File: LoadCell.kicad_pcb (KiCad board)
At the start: 2 copper layers, 50.8 x 18.5 mm, 44 parts, among them J1 M20-8760242, J2 0.100_1X4, J3 M20-8760242, J4 0.100_1X4, J5 M20-8760242, J6 0.100_1X4, J7 M20-8760242, J8 0.100_1X4, U1 L78L12ABUTR, U2 LM321SN3T1G, U3 L78L12ABUTR, U4 LM321SN3T1G, U5 L78L12ABUTR, U6 LM321SN3T1G, U7 L78L12ABUTR, U8 LM321SN3T1G

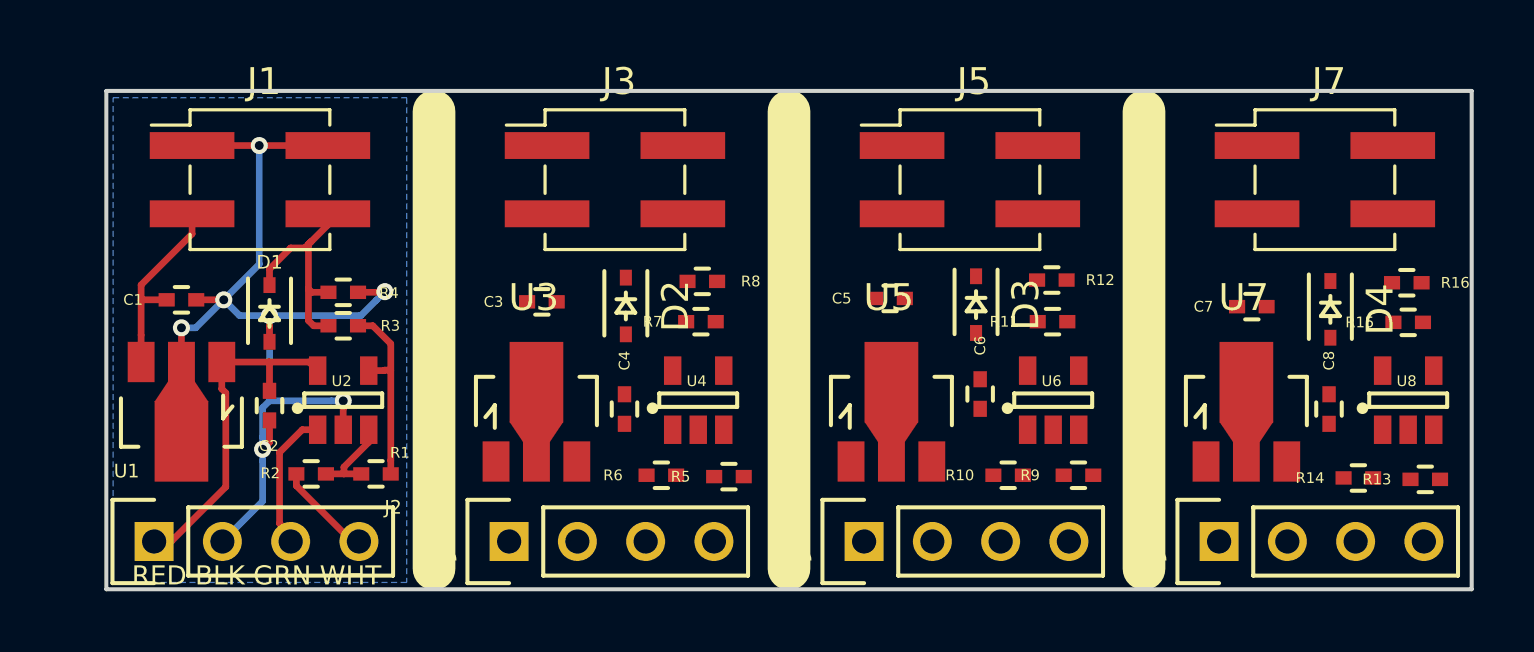
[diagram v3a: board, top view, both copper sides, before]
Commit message: Changed load cell termination pads
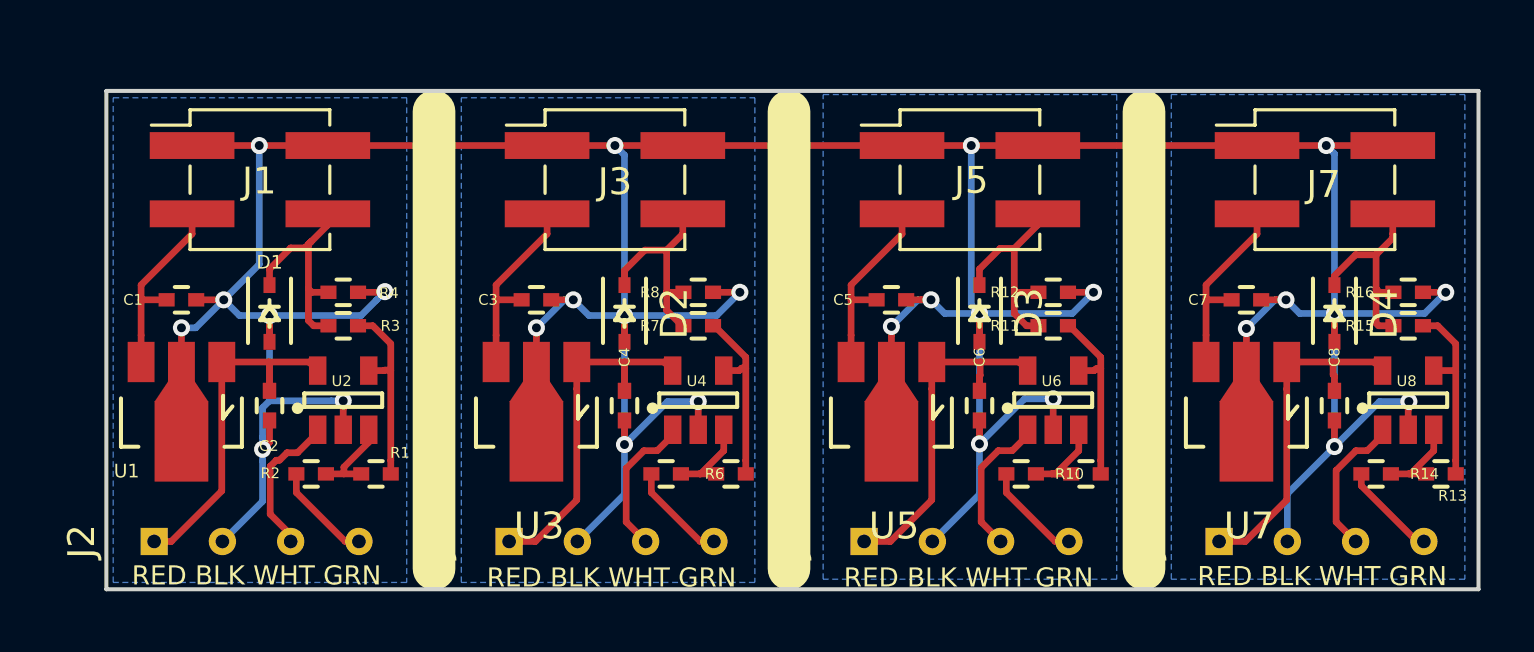
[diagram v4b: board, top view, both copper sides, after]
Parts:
- J2, J4, J6, J8: footprint _Connector:0.100_1x4_small -> _Connector:0.100_1x4_micro
- moved R14 0.68 mm to (148.8, 97.3), turned to 180 degrees
- moved R13 0.62 mm to (151.3, 97.3), turned to 180 degrees
- moved R10 0.49 mm to (135.6, 97.3), turned to 180 degrees
- moved R12 0.46 mm to (136.8, 90.6), turned to 0 degrees
- moved R8 0.43 mm to (123.6, 90.6), turned to 0 degrees
- moved C6 0.43 mm to (134.1, 94.8)
- moved R16 0.36 mm to (150.0, 90.6), turned to 0 degrees
- moved D3 0.35 mm to (134.1, 91.3)
- moved C7 0.33 mm to (144.0, 90.8)
- moved R9 0.28 mm to (138.0, 97.3), turned to 180 degrees
- moved D2 0.28 mm to (120.9, 91.3)
- moved C8 0.24 mm to (147.3, 94.8)
- moved C3 0.22 mm to (117.6, 90.8)
- moved D4 0.22 mm to (147.3, 91.3)
- moved R6 0.18 mm to (122.4, 97.3), turned to 180 degrees
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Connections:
- J2 pad 3: /Main Sheet/GRN -> /Main Sheet/VL+
- J2 pad 4: /Main Sheet/WHT -> /Main Sheet/GRN
- R2 pad 2: /Main Sheet/WHT -> /Main Sheet/GRN
- U2 pad 1: /Main Sheet/GRN -> /Main Sheet/VL+
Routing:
- net GND: track 42.4 -> 191.8 mm, vias 7 -> 28
- net Net-(C8-Pad1): track 0.00 -> 13.1 mm
- net Net-(C6-Pad1): track 0.00 -> 13.1 mm
- net Net-(C4-Pad1): track 0.00 -> 13.1 mm
- net Net-(D3-Pad1): track 0.00 -> 8.27 mm
- net Net-(D4-Pad1): track 0.00 -> 7.93 mm
- net Net-(D2-Pad1): track 0.00 -> 7.75 mm
- net Net-(C3-Pad1): track 0.00 -> 7.26 mm
- net Net-(C7-Pad1): track 0.00 -> 7.26 mm
- net Net-(C5-Pad1): track 0.00 -> 7.25 mm
- net Net-(R13-Pad1): track 0.00 -> 7.17 mm
- net Net-(R5-Pad1): track 0.00 -> 6.90 mm
- net Net-(R11-Pad2): track 0.00 -> 6.89 mm
- net /Main Sheet/VL+: track 0.00 -> 5.50 mm
- net Net-(J6-Pad3): track 0.00 -> 5.48 mm
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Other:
- board size 50.8 x 18.5 mm -> 51.1 x 18.5 mm
- board text added: "RED BLK WHT GRN"
- board text removed: "RED BLK GRN WHT"

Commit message: Added fiducials, final check
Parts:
- added FID1: Fiducial_Top, _Connector:Fiducial_0.040_Top, F.Cu at (102.5, 84.3)
- added FID2: Fiducial_Top, _Connector:Fiducial_0.040_Top, F.Cu at (151.7, 84.1)
- added FID3: Fiducial_Top, _Connector:Fiducial_0.040_Top, F.Cu at (151.7, 100.9)
- added REF**: Mousebites_0.020, _Connector:Mousebites__0.020, F.Cu at (140.2, 88.6)
- added REF**: Mousebites_0.020, _Connector:Mousebites__0.020, F.Cu at (140.2, 93.7)
- added REF**: Mousebites_0.020, _Connector:Mousebites__0.020, F.Cu at (140.2, 98.8)
- added REF**: Mousebites_0.020, _Connector:Mousebites__0.020, F.Cu at (127.0, 88.6)
- added REF**: Mousebites_0.020, _Connector:Mousebites__0.020, F.Cu at (127.0, 93.7)
- added REF**: Mousebites_0.020, _Connector:Mousebites__0.020, F.Cu at (127.0, 98.8)
- added REF**: Mousebites_0.020, _Connector:Mousebites__0.020, F.Cu at (113.8, 88.6)
- added REF**: Mousebites_0.020, _Connector:Mousebites__0.020, F.Cu at (113.8, 93.7)
- added REF**: Mousebites_0.020, _Connector:Mousebites__0.020, F.Cu at (113.8, 98.8)
- added mb**: Mousebite_0.020, _Connector:Mousebite__0.020, F.Cu at (140.2, 85.6)
- added mb**: Mousebite_0.020, _Connector:Mousebite__0.020, F.Cu at (140.2, 84.6)
- added mb**: Mousebite_0.020, _Connector:Mousebite__0.020, F.Cu at (127.0, 85.6)
- added mb**: Mousebite_0.020, _Connector:Mousebite__0.020, F.Cu at (127.0, 84.6)
- added mb**: Mousebite_0.020, _Connector:Mousebite__0.020, F.Cu at (113.8, 84.6)
- added mb**: Mousebite_0.020, _Connector:Mousebite__0.020, F.Cu at (113.8, 85.6)
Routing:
- net GND: track 191.8 -> 210.7 mm

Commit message: Submitted to OSHpark
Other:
- rule pad_to_mask_clearance: 0.2 -> 0.0762
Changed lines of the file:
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@@
     (links 99)
     (no_connects 0)
-    (area 101.524999 82.982999 152.729001 101.675001)
+    (area 99.1 81.637 154.910797 105.713857)
     (thickness 1.6)
     (drawings 9)
@@
     (pad_size 1.45 1.45)
     (pad_drill 0.9)
-    (pad_to_mask_clearance 0.2)
+    (pad_to_mask_clearance 0.0762)
+    (solder_mask_min_width 0.0254)
+    (pad_to_paste_clearance -0.0254)
     (aux_axis_origin 101.6 101.6)
     (visible_elements FFFFFF7F)
     (pcbplotparams
-      (layerselection 0x00030_80000001)
+      (layerselection 0x010fc_80000001)
       (usegerberextensions false)
       (excludeedgelayer true)
@@
       (psnegative false)
       (psa4output false)
-      (plotreference true)
+      (plotreference false)
       (plotvalue true)
       (plotinvisibletext false)
@@
       (outputformat 1)
       (mirror false)
-      (drillshape 1)
+      (drillshape 0)
       (scaleselection 1)
-      (outputdirectory ""))
+      (outputdirectory ProjectOutputs/))
   )
   (net 0 "")

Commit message: Checkpoint
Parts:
- removed the D2 at (120.9, 91.3)
- removed the J4 at (120.4, 99.8)
- removed REF** (x9): Mousebites_0.020, _Connector:Mousebites__0.020
- removed mb** (x6): Mousebite_0.020, _Connector:Mousebite__0.020
- added C10: 1uF, _Passive:C_0603, F.Cu at (132.7, 46.7)
- added C11: 1uF, _Passive:C_0603, F.Cu at (132.7, 48.8)
- added C12: 1uF, _Passive:C_0603, F.Cu at (132.9, 50.8)
- added C13: 1uF, _Passive:C_0603, F.Cu at (132.7, 53.0)
- added C14: 1uF, _Passive:C_0603, F.Cu at (132.9, 54.9)
- added C15: 1uF, _Passive:C_0603, F.Cu at (133.0, 57.0)
- added C16: 1uF, _Passive:C_0603, F.Cu at (133.1, 58.9)
- added C9: 1uF, _Passive:C_0603, F.Cu at (132.6, 44.6)
- added D1: MM3Z3V0ST1G, _Passive:SOD-323, F.Cu at (114.9, 38.5)
- added D5: MM3Z3V0ST1G, _Passive:SOD-323, F.Cu at (114.6, 48.4)
- added D6: MM3Z3V0ST1G, _Passive:SOD-323, F.Cu at (114.4, 51.1)
- added D7: MM3Z3V0ST1G, _Passive:SOD-323, F.Cu at (114.4, 53.7)
- added D8: MM3Z3V0ST1G, _Passive:SOD-323, F.Cu at (114.4, 56.1)
- added J1: M20-8760242, _Connector:Pin_Header_Straight_2x02_Pitch2.54mm_SMD, F.Cu at (107.2, 66.8)
- added J10: M20-8760242, _Connector:Pin_Header_Straight_2x02_Pitch2.54mm_SMD, F.Cu at (120.2, 86.6)
- added J11: 0.100_1X4, _Connector:0.100_1x4_micro, F.Cu at (107.6, 99.2)
- added J12: 0.100_1X4, _Connector:0.100_1x4_micro, F.Cu at (120.7, 99.6)
- added J13: M20-8760242, _Connector:Pin_Header_Straight_2x02_Pitch2.54mm_SMD, F.Cu at (133.6, 86.6)
- added J14: M20-8760242, _Connector:Pin_Header_Straight_2x02_Pitch2.54mm_SMD, F.Cu at (146.3, 86.9)
- added J15: 0.100_1X4, _Connector:0.100_1x4_micro, F.Cu at (133.7, 99.4)
- added J16: 0.100_1X4, _Connector:0.100_1x4_micro, F.Cu at (146.4, 99.4)
- added J9: M20-8760242, _Connector:Pin_Header_Straight_2x02_Pitch2.54mm_SMD, F.Cu at (107.7, 86.6)
- added R17: 390K, _Passive:R_0603, F.Cu at (124.9, 30.6)
- added R18: 1K, _Passive:R_0603, F.Cu at (125.0, 32.8)
- added R19: 390K, _Passive:R_0603, F.Cu at (124.9, 34.8)
- added R20: 1K, _Passive:R_0603, F.Cu at (124.9, 36.8)
- added R21: 1K, _Passive:R_0603, F.Cu at (124.9, 39.0)
- added R22: 270K, _Passive:R_0603, F.Cu at (124.9, 40.8)
- added R23: 1K, _Passive:R_0603, F.Cu at (124.9, 42.8)
- added R24: 270K, _Passive:R_0603, F.Cu at (124.9, 44.8)
- added R25: 390K, _Passive:R_0603, F.Cu at (124.9, 46.9)
- added R26: 1K, _Passive:R_0603, F.Cu at (124.9, 48.9)
- added R27: 390K, _Passive:R_0603, F.Cu at (124.7, 50.8)
- added R28: 1K, _Passive:R_0603, F.Cu at (124.7, 52.8)
- added R29: 1K, _Passive:R_0603, F.Cu at (124.7, 55.1)
- added R30: 270K, _Passive:R_0603, F.Cu at (124.9, 57.1)
- added R31: 1K, _Passive:R_0603, F.Cu at (124.7, 59.2)
- added R32: 270K, _Passive:R_0603, F.Cu at (124.8, 61.3)
- C1, C2, C3, C4, C5, C6, C7, C8: footprint _Passive:C_0402 -> _Passive:C_0603
- J3, J7: value M20-8760242 -> 0.100_1X4; footprint _Connector:Pin_Header_Straight_2x02_Pitch2.54mm_SMD -> _Connector:0.100_1x4_micro
- J6: value 0.100_1X4 -> M20-8760242; footprint _Connector:0.100_1x4_micro -> _Connector:Pin_Header_Straight_2x02_Pitch2.54mm_SMD
- R1, R9: value 270K -> 390K; footprint _Passive:R_0402 -> _Passive:R_0603
- R10, R2: footprint _Passive:R_0402 -> _Passive:R_0603
- R11, R3: value 100R -> 390K; footprint _Passive:R_0402 -> _Passive:R_0603
- R12, R15, R4, R7: value 100R -> 1K; footprint _Passive:R_0402 -> _Passive:R_0603
- R13, R5: value 270K -> 1K; footprint _Passive:R_0402 -> _Passive:R_0603
- R14, R6: value 1K -> 270K; footprint _Passive:R_0402 -> _Passive:R_0603
- R16, R8: value 100R -> 270K; footprint _Passive:R_0402 -> _Passive:R_0603
- U1, U3, U5, U7: value L78L12ABUTR -> MCP6002; footprint _Active:SOT89-3 -> Housings_SSOP:TSSOP-8_4.4x3mm_Pitch0.65mm
- U2, U4, U6, U8: value LM321SN3T1G -> MCP6002; footprint _Active:SOT-23-5 -> Housings_SSOP:TSSOP-8_4.4x3mm_Pitch0.65mm
- moved R2 67.7 mm to (120.7, 30.6), turned to 0 degrees
- moved R5 62.5 mm to (120.5, 34.9), turned to 0 degrees
- moved C4 61.6 mm to (132.7, 34.3), turned to 0 degrees
- moved R6 60.2 mm to (120.7, 37.1), turned to 0 degrees
- moved R4 58.7 mm to (120.7, 32.8)
- moved R9 56.9 mm to (120.5, 43.2), turned to 0 degrees
- moved C6 56.4 mm to (132.6, 38.4), turned to 0 degrees
- moved D4 55.8 mm to (114.8, 46.0), turned to 0 degrees
- moved R13 55.7 mm to (120.3, 51.1), turned to 0 degrees
- moved C5 54.5 mm to (132.6, 36.3)
- moved C8 54.4 mm to (132.6, 42.4), turned to 0 degrees
- moved R10 54.3 mm to (120.4, 45.2), turned to 0 degrees
- moved R7 52.8 mm to (120.7, 39.1)
- moved R14 52.7 mm to (120.2, 53.1), turned to 0 degrees
- moved C7 51.7 mm to (132.6, 40.4)
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- renumbered D1 to D2, J1 to J2, J2 to J4
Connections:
- C1 pad 1: /Main Sheet/Vin -> /Main Sheet/Vout
- C1 pad 2: GND -> /Main Sheet/BLK
- C2 pad 1: /Main Sheet/RED -> /Main Sheet/Vout
- C2 pad 2: GND -> /Main Sheet/BLK
- C3 pad 1: Net-(C3-Pad1) -> /Main Sheet/RED
- C3 pad 2: GND -> /Main Sheet/BLK
- C4 pad 1: Net-(C4-Pad1) -> /Main Sheet/RED
- C4 pad 2: GND -> /Main Sheet/BLK
- C5 pad 1: Net-(C5-Pad1) -> /Main Sheet/Vout
- C5 pad 2: GND -> /Main Sheet/BLK
- C6 pad 1: Net-(C6-Pad1) -> /Main Sheet/Vout
- C6 pad 2: GND -> /Main Sheet/BLK
- C7 pad 1: Net-(C7-Pad1) -> /Main Sheet/RED
- C7 pad 2: GND -> /Main Sheet/BLK
- C8 pad 1: Net-(C8-Pad1) -> /Main Sheet/RED
- C8 pad 2: GND -> /Main Sheet/BLK
- D2 pad 2: GND -> /Main Sheet/BLK
- D3 pad 1: Net-(D3-Pad1) -> /Main Sheet/Vout
- D3 pad 2: GND -> /Main Sheet/BLK
- D4 pad 1: Net-(D4-Pad1) -> /Main Sheet/Vout
- D4 pad 2: GND -> /Main Sheet/BLK
- FID1 pad 1: Net-(FID1-Pad1) -> (no net)
- FID2 pad 1: Net-(FID2-Pad1) -> (no net)
- FID3 pad 1: Net-(FID3-Pad1) -> (no net)
- J2 pad 1: GND -> /Main Sheet/BLK
- J2 pad 2: GND -> /Main Sheet/BLK
- J2 pad 3: /Main Sheet/Vin -> /Main Sheet/RED
- J3 pad 1: GND -> /Main Sheet/RED
- J3 pad 2: GND -> /Main Sheet/BLK
- J3 pad 3: Net-(C3-Pad1) -> /Main Sheet/WHT
- J3 pad 4: Net-(D2-Pad1) -> /Main Sheet/GRN
- J4 pad 2: GND -> /Main Sheet/BLK
- J4 pad 3: /Main Sheet/VL+ -> /Main Sheet/WHT
- J5 pad 1: GND -> /Main Sheet/BLK
- J5 pad 2: GND -> /Main Sheet/BLK
- J5 pad 3: Net-(C5-Pad1) -> /Main Sheet/RED
- J5 pad 4: Net-(D3-Pad1) -> /Main Sheet/Vout
- J6 pad 1: Net-(C6-Pad1) -> /Main Sheet/BLK
- J6 pad 2: GND -> /Main Sheet/BLK
- J6 pad 3: Net-(J6-Pad3) -> /Main Sheet/RED
- J6 pad 4: Net-(J6-Pad4) -> /Main Sheet/Vout
- J7 pad 1: GND -> /Main Sheet/RED
- J7 pad 2: GND -> /Main Sheet/BLK
- J7 pad 3: Net-(C7-Pad1) -> /Main Sheet/WHT
- J7 pad 4: Net-(D4-Pad1) -> /Main Sheet/GRN
- J8 pad 1: Net-(C8-Pad1) -> /Main Sheet/RED
- J8 pad 2: GND -> /Main Sheet/BLK
- J8 pad 3: Net-(J8-Pad3) -> /Main Sheet/WHT
- J8 pad 4: Net-(J8-Pad4) -> /Main Sheet/GRN
- R1 pad 1: /Main Sheet/Vopo -> Net-(R1-Pad1)
- R1 pad 2: /Main Sheet/VL- -> Net-(R1-Pad2)
- R10 pad 2: Net-(J6-Pad4) -> /Main Sheet/Vout
- R11 pad 1: Net-(D3-Pad1) -> Net-(R11-Pad1)
- R12 pad 1: Net-(D3-Pad1) -> Net-(R12-Pad1)
- R12 pad 2: GND -> /Main Sheet/Vout
- R13 pad 1: Net-(R13-Pad1) -> /Main Sheet/Vout
- R14 pad 1: Net-(R13-Pad2) -> /Main Sheet/BLK
- R14 pad 2: Net-(J8-Pad4) -> Net-(R10-Pad1)
- R15 pad 1: Net-(D4-Pad1) -> /Main Sheet/Vout
- R15 pad 2: Net-(R13-Pad1) -> Net-(R11-Pad1)
- R16 pad 1: Net-(D4-Pad1) -> /Main Sheet/BLK
- R16 pad 2: GND -> Net-(R12-Pad1)
- R2 pad 1: /Main Sheet/VL- -> Net-(R2-Pad1)
- R2 pad 2: /Main Sheet/GRN -> /Main Sheet/Vout
- R3 pad 1: /Main Sheet/Vout -> Net-(R3-Pad1)
- R3 pad 2: /Main Sheet/Vopo -> Net-(R3-Pad2)
- R4 pad 1: /Main Sheet/Vout -> Net-(R4-Pad1)
- R4 pad 2: GND -> /Main Sheet/Vout
- R5 pad 1: Net-(R5-Pad1) -> /Main Sheet/Vout
- R5 pad 2: Net-(R5-Pad2) -> Net-(R1-Pad1)
- R6 pad 1: Net-(R5-Pad2) -> /Main Sheet/BLK
- R6 pad 2: Net-(J4-Pad4) -> Net-(R2-Pad1)
- R7 pad 1: Net-(D2-Pad1) -> /Main Sheet/Vout
- R7 pad 2: Net-(R5-Pad1) -> Net-(R3-Pad1)
- R8 pad 1: Net-(D2-Pad1) -> /Main Sheet/BLK
- R8 pad 2: GND -> Net-(R4-Pad1)
- R9 pad 1: Net-(R11-Pad2) -> Net-(R13-Pad2)
- R9 pad 2: Net-(R10-Pad1) -> Net-(R9-Pad2)
- U1 pad 1: /Main Sheet/RED -> Net-(R1-Pad2)
- U1 pad 2: GND -> Net-(R1-Pad1)
- U1 pad 3: /Main Sheet/Vin -> /Main Sheet/GRN
- U2 pad 1: /Main Sheet/VL+ -> Net-(R3-Pad2)
- U2 pad 2: GND -> Net-(R3-Pad1)
- U2 pad 3: /Main Sheet/VL- -> /Main Sheet/GRN
- U2 pad 4: /Main Sheet/Vopo -> /Main Sheet/BLK
- U2 pad 5: /Main Sheet/RED -> /Main Sheet/WHT
- U3 pad 1: Net-(C4-Pad1) -> Net-(R9-Pad2)
- U3 pad 2: GND -> Net-(R13-Pad2)
- U3 pad 3: Net-(C3-Pad1) -> /Main Sheet/GRN
- U4 pad 1: Net-(J4-Pad3) -> Net-(R11-Pad2)
- U4 pad 2: GND -> Net-(R11-Pad1)
- U4 pad 3: Net-(R5-Pad2) -> /Main Sheet/GRN
- U4 pad 4: Net-(R5-Pad1) -> /Main Sheet/BLK
- U4 pad 5: Net-(C4-Pad1) -> /Main Sheet/WHT
- U5 pad 1: Net-(C6-Pad1) -> Net-(R17-Pad2)
- U5 pad 2: GND -> Net-(R17-Pad1)
- U5 pad 3: Net-(C5-Pad1) -> /Main Sheet/GRN
- U6 pad 1: Net-(J6-Pad3) -> Net-(R19-Pad2)
- U6 pad 2: GND -> Net-(R19-Pad1)
- U6 pad 3: Net-(R10-Pad1) -> /Main Sheet/GRN
- U6 pad 4: Net-(R11-Pad2) -> /Main Sheet/BLK
- U6 pad 5: Net-(C6-Pad1) -> /Main Sheet/WHT
- U7 pad 1: Net-(C8-Pad1) -> Net-(R25-Pad2)
- U7 pad 2: GND -> Net-(R25-Pad1)
- U7 pad 3: Net-(C7-Pad1) -> /Main Sheet/GRN
- U8 pad 1: Net-(J8-Pad3) -> Net-(R27-Pad2)
- U8 pad 2: GND -> Net-(R27-Pad1)
- U8 pad 3: Net-(R13-Pad2) -> /Main Sheet/GRN
- U8 pad 4: Net-(R13-Pad1) -> /Main Sheet/BLK
- U8 pad 5: Net-(C8-Pad1) -> /Main Sheet/WHT
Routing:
- net GND: track 210.7 -> 0.00 mm, vias 28 -> 0
- net Net-(C8-Pad1): track 13.1 -> 0.00 mm
- net Net-(C6-Pad1): track 13.1 -> 0.00 mm
- net Net-(C4-Pad1): track 13.1 -> 0.00 mm
- net /Main Sheet/RED: track 12.9 -> 0.00 mm
- net /Main Sheet/Vout: track 8.46 -> 0.00 mm
- net Net-(D3-Pad1): track 8.27 -> 0.00 mm
- net Net-(D4-Pad1): track 7.93 -> 0.00 mm
- net Net-(D2-Pad1): track 7.75 -> 0.00 mm
- net Net-(C3-Pad1): track 7.26 -> 0.00 mm
- net Net-(C7-Pad1): track 7.26 -> 0.00 mm
- net /Main Sheet/Vin: track 7.25 -> 0.00 mm
- net Net-(C5-Pad1): track 7.25 -> 0.00 mm
- net Net-(R5-Pad1): track 7.18 -> 0.00 mm
- net Net-(R13-Pad1): track 7.17 -> 0.00 mm
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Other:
- board size 51.1 x 18.5 mm -> 51.1 x 38.1 mm

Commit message: Checkpoint - first unit laid out
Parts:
- R14, R16, R22, R24, R30, R32, R6, R8: value 270K -> 390K
- moved R2 44.0 mm to (104.6, 71.6), turned to 90 degrees
- moved R5 38.7 mm to (108.2, 71.6), turned to 270 degrees
- moved R6 37.4 mm to (106.4, 71.6), turned to 270 degrees
- moved D1 37.3 mm to (111.8, 75.7), turned to 270 degrees
- moved C1 18.3 mm to (111.8, 71.6), turned to 270 degrees
- moved R1 16.0 mm to (110.0, 71.6), turned to 90 degrees
- moved C3 13.5 mm to (102.7, 71.6), turned to 90 degrees
- moved R3 7.71 mm to (114.9, 61.3)
- moved C2 6.86 mm to (111.4, 60.1)
- moved U1 0.69 mm to (106.8, 75.8), turned to 180 degrees
- moved FID1 0.28 mm to (102.5, 64.4)
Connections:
- C10 pad 1: /Main Sheet/Vout -> Net-(C10-Pad1)
- C10 pad 2: /Main Sheet/BLK -> Net-(C10-Pad2)
- C11 pad 1: /Main Sheet/RED -> Net-(C11-Pad1)
- C11 pad 2: /Main Sheet/BLK -> Net-(C11-Pad2)
- C12 pad 1: /Main Sheet/RED -> Net-(C12-Pad1)
- C12 pad 2: /Main Sheet/BLK -> Net-(C10-Pad2)
- C13 pad 1: /Main Sheet/Vout -> Net-(C13-Pad1)
- C13 pad 2: /Main Sheet/BLK -> Net-(C13-Pad2)
- C14 pad 1: /Main Sheet/Vout -> Net-(C14-Pad1)
- C14 pad 2: /Main Sheet/BLK -> Net-(C14-Pad2)
- C15 pad 1: /Main Sheet/RED -> Net-(C15-Pad1)
- C15 pad 2: /Main Sheet/BLK -> Net-(C13-Pad2)
- C16 pad 1: /Main Sheet/RED -> Net-(C16-Pad1)
- C16 pad 2: /Main Sheet/BLK -> Net-(C14-Pad2)
- C2 pad 1: /Main Sheet/Vout -> Net-(C2-Pad1)
- C2 pad 2: /Main Sheet/BLK -> Net-(C2-Pad2)
- C4 pad 1: /Main Sheet/RED -> Net-(C4-Pad1)
- C4 pad 2: /Main Sheet/BLK -> Net-(C2-Pad2)
- C5 pad 1: /Main Sheet/Vout -> Net-(C5-Pad1)
- C5 pad 2: /Main Sheet/BLK -> Net-(C5-Pad2)
- C6 pad 1: /Main Sheet/Vout -> Net-(C6-Pad1)
- C6 pad 2: /Main Sheet/BLK -> Net-(C6-Pad2)
- C7 pad 1: /Main Sheet/RED -> Net-(C7-Pad1)
- C7 pad 2: /Main Sheet/BLK -> Net-(C5-Pad2)
- C8 pad 1: /Main Sheet/RED -> Net-(C8-Pad1)
- C8 pad 2: /Main Sheet/BLK -> Net-(C6-Pad2)
- C9 pad 1: /Main Sheet/Vout -> Net-(C9-Pad1)
- C9 pad 2: /Main Sheet/BLK -> Net-(C11-Pad2)
- D2 pad 1: /Main Sheet/Vout -> Net-(C2-Pad1)
- D2 pad 2: /Main Sheet/BLK -> Net-(C2-Pad2)
- D3 pad 1: /Main Sheet/Vout -> Net-(C5-Pad1)
- D3 pad 2: /Main Sheet/BLK -> Net-(C5-Pad2)
- D4 pad 1: /Main Sheet/Vout -> Net-(C6-Pad1)
- D4 pad 2: /Main Sheet/BLK -> Net-(C6-Pad2)
- D5 pad 1: /Main Sheet/Vout -> Net-(C9-Pad1)
- D5 pad 2: /Main Sheet/BLK -> Net-(C11-Pad2)
- D6 pad 1: /Main Sheet/Vout -> Net-(C10-Pad1)
- D6 pad 2: /Main Sheet/BLK -> Net-(C10-Pad2)
- D7 pad 1: /Main Sheet/Vout -> Net-(C13-Pad1)
- D7 pad 2: /Main Sheet/BLK -> Net-(C13-Pad2)
- D8 pad 1: /Main Sheet/Vout -> Net-(C14-Pad1)
- D8 pad 2: /Main Sheet/BLK -> Net-(C14-Pad2)
- J10 pad 1: /Main Sheet/BLK -> Net-(C10-Pad2)
- J10 pad 2: /Main Sheet/BLK -> Net-(C10-Pad2)
- J10 pad 3: /Main Sheet/RED -> Net-(C12-Pad1)
- J10 pad 4: /Main Sheet/Vout -> Net-(C10-Pad1)
- J11 pad 1: /Main Sheet/RED -> Net-(C11-Pad1)
- J11 pad 2: /Main Sheet/BLK -> Net-(C11-Pad2)
- J11 pad 3: /Main Sheet/WHT -> Net-(J11-Pad3)
- J11 pad 4: /Main Sheet/GRN -> Net-(J11-Pad4)
- J12 pad 1: /Main Sheet/RED -> Net-(C12-Pad1)
- J12 pad 2: /Main Sheet/BLK -> Net-(C10-Pad2)
- J12 pad 3: /Main Sheet/WHT -> Net-(J12-Pad3)
- J12 pad 4: /Main Sheet/GRN -> Net-(J12-Pad4)
- J13 pad 1: /Main Sheet/BLK -> Net-(C13-Pad2)
- J13 pad 2: /Main Sheet/BLK -> Net-(C13-Pad2)
- J13 pad 3: /Main Sheet/RED -> Net-(C15-Pad1)
- J13 pad 4: /Main Sheet/Vout -> Net-(C13-Pad1)
- J14 pad 1: /Main Sheet/BLK -> Net-(C14-Pad2)
- J14 pad 2: /Main Sheet/BLK -> Net-(C14-Pad2)
- J14 pad 3: /Main Sheet/RED -> Net-(C16-Pad1)
- J14 pad 4: /Main Sheet/Vout -> Net-(C14-Pad1)
- J15 pad 1: /Main Sheet/RED -> Net-(C15-Pad1)
- J15 pad 2: /Main Sheet/BLK -> Net-(C13-Pad2)
- J15 pad 3: /Main Sheet/WHT -> Net-(J15-Pad3)
- J15 pad 4: /Main Sheet/GRN -> Net-(J15-Pad4)
- J16 pad 1: /Main Sheet/RED -> Net-(C16-Pad1)
- J16 pad 2: /Main Sheet/BLK -> Net-(C14-Pad2)
- J16 pad 3: /Main Sheet/WHT -> Net-(J16-Pad3)
- J16 pad 4: /Main Sheet/GRN -> Net-(J16-Pad4)
- J2 pad 1: /Main Sheet/BLK -> Net-(C2-Pad2)
- J2 pad 2: /Main Sheet/BLK -> Net-(C2-Pad2)
- J2 pad 3: /Main Sheet/RED -> Net-(C4-Pad1)
- J2 pad 4: /Main Sheet/Vout -> Net-(C2-Pad1)
- J4 pad 1: /Main Sheet/RED -> Net-(C4-Pad1)
- J4 pad 2: /Main Sheet/BLK -> Net-(C2-Pad2)
- J4 pad 3: /Main Sheet/WHT -> Net-(J4-Pad3)
- J4 pad 4: /Main Sheet/GRN -> Net-(J4-Pad4)
- J5 pad 1: /Main Sheet/BLK -> Net-(C5-Pad2)
- J5 pad 2: /Main Sheet/BLK -> Net-(C5-Pad2)
- J5 pad 3: /Main Sheet/RED -> Net-(C7-Pad1)
- J5 pad 4: /Main Sheet/Vout -> Net-(C5-Pad1)
- J6 pad 1: /Main Sheet/BLK -> Net-(C6-Pad2)
- J6 pad 2: /Main Sheet/BLK -> Net-(C6-Pad2)
- J6 pad 3: /Main Sheet/RED -> Net-(C8-Pad1)
- J6 pad 4: /Main Sheet/Vout -> Net-(C6-Pad1)
- J7 pad 1: /Main Sheet/RED -> Net-(C7-Pad1)
- J7 pad 2: /Main Sheet/BLK -> Net-(C5-Pad2)
- J7 pad 3: /Main Sheet/WHT -> Net-(J7-Pad3)
- J7 pad 4: /Main Sheet/GRN -> Net-(J7-Pad4)
- J8 pad 1: /Main Sheet/RED -> Net-(C8-Pad1)
- J8 pad 2: /Main Sheet/BLK -> Net-(C6-Pad2)
- J8 pad 3: /Main Sheet/WHT -> Net-(J8-Pad3)
- J8 pad 4: /Main Sheet/GRN -> Net-(J8-Pad4)
- J9 pad 1: /Main Sheet/BLK -> Net-(C11-Pad2)
- J9 pad 2: /Main Sheet/BLK -> Net-(C11-Pad2)
- J9 pad 3: /Main Sheet/RED -> Net-(C11-Pad1)
- J9 pad 4: /Main Sheet/Vout -> Net-(C9-Pad1)
- R10 pad 2: /Main Sheet/Vout -> Net-(C5-Pad1)
- R12 pad 2: /Main Sheet/Vout -> Net-(C6-Pad1)
- R13 pad 1: /Main Sheet/Vout -> Net-(C5-Pad1)
- R14 pad 1: /Main Sheet/BLK -> Net-(C5-Pad2)
- R15 pad 1: /Main Sheet/Vout -> Net-(C6-Pad1)
- R16 pad 1: /Main Sheet/BLK -> Net-(C6-Pad2)
- R18 pad 2: /Main Sheet/Vout -> Net-(C9-Pad1)
- R20 pad 2: /Main Sheet/Vout -> Net-(C10-Pad1)
- R21 pad 1: /Main Sheet/Vout -> Net-(C9-Pad1)
- R22 pad 1: /Main Sheet/BLK -> Net-(C11-Pad2)
- R23 pad 1: /Main Sheet/Vout -> Net-(C10-Pad1)
- R24 pad 1: /Main Sheet/BLK -> Net-(C10-Pad2)
- R26 pad 2: /Main Sheet/Vout -> Net-(C13-Pad1)
- R28 pad 2: /Main Sheet/Vout -> Net-(C14-Pad1)
- R29 pad 1: /Main Sheet/Vout -> Net-(C13-Pad1)
- R30 pad 1: /Main Sheet/BLK -> Net-(C13-Pad2)
- R31 pad 1: /Main Sheet/Vout -> Net-(C14-Pad1)
- R32 pad 1: /Main Sheet/BLK -> Net-(C14-Pad2)
- R4 pad 2: /Main Sheet/Vout -> Net-(C2-Pad1)
- R7 pad 1: /Main Sheet/Vout -> Net-(C2-Pad1)
- R8 pad 1: /Main Sheet/BLK -> Net-(C2-Pad2)
- U2 pad 3: /Main Sheet/GRN -> Net-(J4-Pad4)
- U2 pad 4: /Main Sheet/BLK -> Net-(C2-Pad2)
- U2 pad 5: /Main Sheet/WHT -> Net-(J4-Pad3)
- U2 pad 7: /Main Sheet/Vout -> Net-(C2-Pad1)
- U2 pad 8: /Main Sheet/RED -> Net-(C4-Pad1)
- U3 pad 3: /Main Sheet/GRN -> Net-(J7-Pad4)
- U3 pad 4: /Main Sheet/BLK -> Net-(C5-Pad2)
- U3 pad 5: /Main Sheet/WHT -> Net-(J7-Pad3)
- U3 pad 7: /Main Sheet/Vout -> Net-(C5-Pad1)
- U3 pad 8: /Main Sheet/RED -> Net-(C7-Pad1)
- U4 pad 3: /Main Sheet/GRN -> Net-(J8-Pad4)
- U4 pad 4: /Main Sheet/BLK -> Net-(C6-Pad2)
- U4 pad 5: /Main Sheet/WHT -> Net-(J8-Pad3)
- U4 pad 7: /Main Sheet/Vout -> Net-(C6-Pad1)
- U4 pad 8: /Main Sheet/RED -> Net-(C8-Pad1)
- U5 pad 3: /Main Sheet/GRN -> Net-(J11-Pad4)
- U5 pad 4: /Main Sheet/BLK -> Net-(C11-Pad2)
- U5 pad 5: /Main Sheet/WHT -> Net-(J11-Pad3)
- U5 pad 7: /Main Sheet/Vout -> Net-(C9-Pad1)
- U5 pad 8: /Main Sheet/RED -> Net-(C11-Pad1)
- U6 pad 3: /Main Sheet/GRN -> Net-(J12-Pad4)
- U6 pad 4: /Main Sheet/BLK -> Net-(C10-Pad2)
- U6 pad 5: /Main Sheet/WHT -> Net-(J12-Pad3)
- U6 pad 7: /Main Sheet/Vout -> Net-(C10-Pad1)
- U6 pad 8: /Main Sheet/RED -> Net-(C12-Pad1)
- U7 pad 3: /Main Sheet/GRN -> Net-(J15-Pad4)
- U7 pad 4: /Main Sheet/BLK -> Net-(C13-Pad2)
- U7 pad 5: /Main Sheet/WHT -> Net-(J15-Pad3)
- U7 pad 7: /Main Sheet/Vout -> Net-(C13-Pad1)
- U7 pad 8: /Main Sheet/RED -> Net-(C15-Pad1)
- U8 pad 3: /Main Sheet/GRN -> Net-(J16-Pad4)
- U8 pad 4: /Main Sheet/BLK -> Net-(C14-Pad2)
- U8 pad 5: /Main Sheet/WHT -> Net-(J16-Pad3)
- U8 pad 7: /Main Sheet/Vout -> Net-(C14-Pad1)
- U8 pad 8: /Main Sheet/RED -> Net-(C16-Pad1)
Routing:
- net /Main Sheet/BLK: track 0.00 -> 37.7 mm, vias 0 -> 6
- net /Main Sheet/Vout: track 0.00 -> 23.8 mm
- net /Main Sheet/RED: track 0.00 -> 16.1 mm
- net /Main Sheet/WHT: track 0.00 -> 8.13 mm
- net Net-(R2-Pad1): track 0.00 -> 7.87 mm
- net Net-(R1-Pad2): track 0.00 -> 7.69 mm
- net Net-(R1-Pad1): track 0.00 -> 7.66 mm
- net /Main Sheet/GRN: track 0.00 -> 6.72 mm
- added copper zone on B.Cu, net /Main Sheet/BLK
